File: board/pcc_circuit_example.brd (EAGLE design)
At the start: 52 x 29.1 mm, 18 parts, among them T1 BT138-V

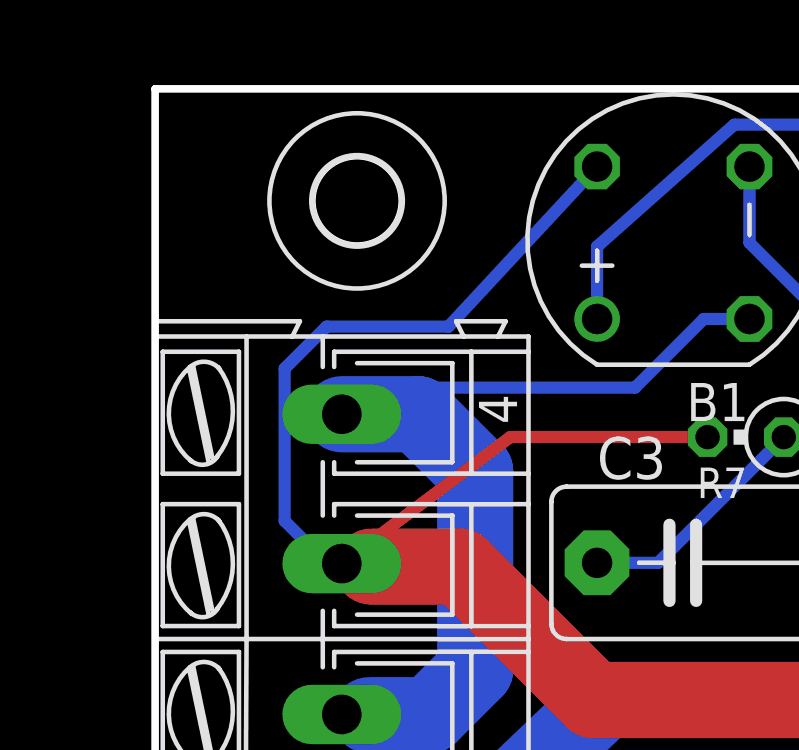
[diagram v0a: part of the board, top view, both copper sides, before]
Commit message: reduce number of drilltools
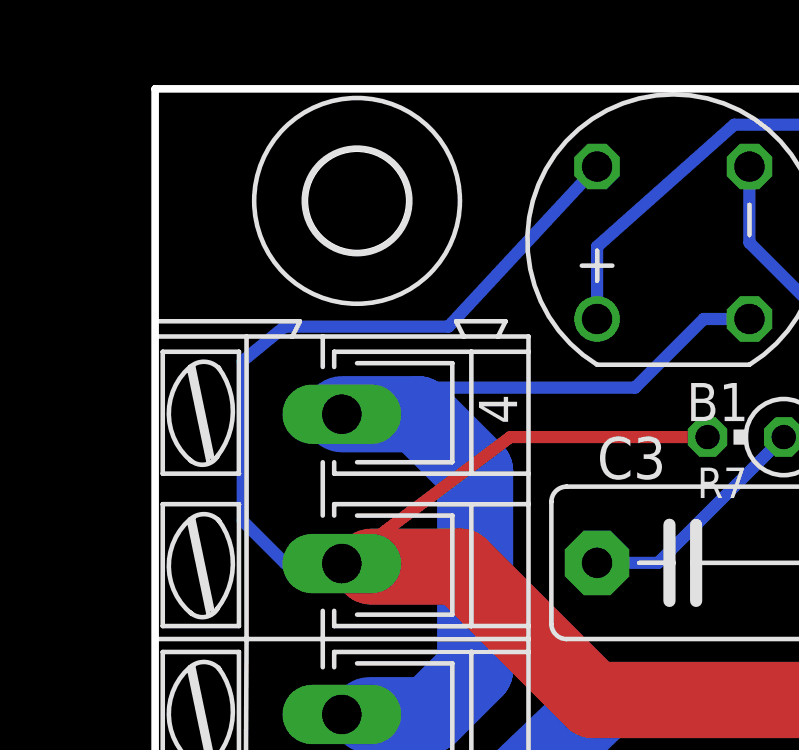
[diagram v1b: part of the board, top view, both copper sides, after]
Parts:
- U$3: device holes:2,8 -> bauteile_jbt:3,3
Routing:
- net AC220V2: track 57.2 -> 60.0 mm
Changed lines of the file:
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@@
 <grid distance="5" unitdist="mil" unit="mil" style="lines" multiple="1" display="yes" altdistance="100" altunitdist="mil" altunit="mil"/>
 <layers>
-<layer number="1" name="Top" color="4" fill="1" visible="yes" active="yes"/>
+<layer number="1" name="Top" color="4" fill="1" visible="no" active="yes"/>
 <layer number="2" name="Route2" color="1" fill="3" visible="no" active="no"/>
 <layer number="3" name="Route3" color="4" fill="3" visible="no" active="no"/>
 <layer number="14" name="Route14" color="1" fill="6" visible="no" active="no"/>
 <layer number="15" name="Route15" color="4" fill="6" visible="no" active="no"/>
-<layer number="16" name="Bottom" color="1" fill="1" visible="no" active="yes"/>
-<layer number="17" name="Pads" color="2" fill="1" visible="no" active="yes"/>
-<layer number="18" name="Vias" color="2" fill="1" visible="no" active="yes"/>
-<layer number="19" name="Unrouted" color="6" fill="1" visible="no" active="yes"/>
+<layer number="16" name="Bottom" color="1" fill="1" visible="yes" active="yes"/>
+<layer number="17" name="Pads" color="2" fill="1" visible="yes" active="yes"/>
+<layer number="18" name="Vias" color="2" fill="1" visible="yes" active="yes"/>
+<layer number="19" name="Unrouted" color="6" fill="1" visible="yes" active="yes"/>
 <layer number="20" name="Dimension" color="15" fill="1" visible="yes" active="yes"/>
-<layer number="21" name="tPlace" color="7" fill="1" visible="yes" active="yes"/>
-<layer number="22" name="bPlace" color="7" fill="1" visible="no" active="yes"/>
+<layer number="21" name="tPlace" color="7" fill="1" visible="no" active="yes"/>
+<layer number="22" name="bPlace" color="7" fill="1" visible="yes" active="yes"/>
 <layer number="23" name="tOrigins" color="15" fill="1" visible="yes" active="yes"/>
-<layer number="24" name="bOrigins" color="15" fill="1" visible="no" active="yes"/>
+<layer number="24" name="bOrigins" color="15" fill="1" visible="yes" active="yes"/>
 <layer number="25" name="tNames" color="7" fill="1" visible="no" active="yes"/>
 <layer number="26" name="bNames" color="7" fill="1" visible="no" active="yes"/>
-<layer number="27" name="tValues" color="7" fill="1" visible="yes" active="yes"/>
-<layer number="28" name="bValues" color="7" fill="1" visible="no" active="yes"/>
-<layer number="29" name="tStop" color="7" fill="3" visible="yes" active="yes"/>
-<layer number="30" name="bStop" color="7" fill="6" visible="no" active="yes"/>
+<layer number="27" name="tValues" color="7" fill="1" visible="no" active="yes"/>
+<layer number="28" name="bValues" color="7" fill="1" visible="yes" active="yes"/>
+<layer number="29" name="tStop" color="7" fill="3" visible="no" active="yes"/>
+<layer number="30" name="bStop" color="7" fill="6" visible="yes" active="yes"/>
 <layer number="31" name="tCream" color="7" fill="4" visible="no" active="yes"/>
 <layer number="32" name="bCream" color="7" fill="5" visible="no" active="yes"/>
@@
 <layer number="37" name="tTest" color="7" fill="1" visible="no" active="yes"/>
 <layer number="38" name="bTest" color="7" fill="1" visible="no" active="yes"/>
-<layer number="39" name="tKeepout" color="4" fill="11" visible="no" active="yes"/>
-<layer number="40" name="bKeepout" color="1" fill="11" visible="no" active="yes"/>
-<layer number="41" name="tRestrict" color="4" fill="10" visible="no" active="yes"/>
-<layer number="42" name="bRestrict" color="1" fill="10" visible="no" active="yes"/>
+<layer number="39" name="tKeepout" color="4" fill="11" visible="yes" active="yes"/>
+<layer number="40" name="bKeepout" color="1" fill="11" visible="yes" active="yes"/>
+<layer number="41" name="tRestrict" color="4" fill="10" visible="yes" active="yes"/>
+<layer number="42" name="bRestrict" color="1" fill="10" visible="yes" active="yes"/>
 <layer number="43" name="vRestrict" color="2" fill="10" visible="no" active="yes"/>
-<layer number="44" name="Drills" color="7" fill="1" visible="yes" active="yes"/>
-<layer number="45" name="Holes" color="7" fill="1" visible="yes" active="yes"/>
-<layer number="46" name="Milling" color="3" fill="1" visible="yes" active="yes"/>
+<layer number="44" name="Drills" color="7" fill="1" visible="no" active="yes"/>
+<layer number="45" name="Holes" color="7" fill="1" visible="no" active="yes"/>
+<layer number="46" name="Milling" color="3" fill="1" visible="no" active="yes"/>
 <layer number="47" name="Measures" color="7" fill="1" visible="no" active="yes"/>
 <layer number="48" name="Document" color="7" fill="1" visible="no" active="yes"/>
@@
 <attribute name="MPN" value="" x="6.223" y="10.795" size="1.778" layer="27" rot="R90" display="off"/>
 </element>
-<element name="U$3" library="holes" package="2,8" value="" x="6.731" y="25.4"/>
+<element name="U$3" library="bauteile_jbt" package="3,3" value="" x="6.731" y="25.4"/>
 <element name="SV1" library="bauteile_jbt" package="FE03-2" value="" x="42.545" y="4.699"/>
 <element name="VCC" library="bauteile_jbt" package="PAD1,6/0,8" value="" x="47.625" y="5.842"/>
@@
 <wire x1="18.415" y1="17.526" x2="11.8364" y2="17.526" width="0.4064" layer="1"/>
 <wire x1="11.8364" y1="17.526" x2="6.223" y2="13.3096" width="0.4064" layer="1"/>
-<wire x1="5.7404" y1="13.3096" x2="4.318" y2="14.732" width="0.4064" layer="16"/>
-<wire x1="4.318" y1="14.732" x2="4.318" y2="19.812" width="0.4064" layer="16"/>
-<wire x1="4.318" y1="19.812" x2="5.715" y2="21.209" width="0.4064" layer="16"/>
-<wire x1="5.715" y1="21.209" x2="9.779" y2="21.209" width="0.4064" layer="16"/>
+<wire x1="4.3434" y1="13.3096" x2="2.921" y2="14.732" width="0.4064" layer="16"/>
+<wire x1="2.921" y1="14.732" x2="2.921" y2="20.066" width="0.4064" layer="16"/>
+<wire x1="2.921" y1="20.066" x2="4.318" y2="21.209" width="0.4064" layer="16"/>
+<wire x1="4.318" y1="21.209" x2="9.779" y2="21.209" width="0.4064" layer="16"/>
 <wire x1="9.779" y1="21.209" x2="14.732" y2="26.543" width="0.4064" layer="16"/>
 <wire x1="23.622" y1="4.445" x2="23.622" y2="7.239" width="2.54" layer="1"/>
@@
 <wire x1="10.16" y1="13.208" x2="7.2136" y2="13.208" width="2.54" layer="1"/>
 <wire x1="7.2136" y1="13.208" x2="6.223" y2="13.3096" width="1.9304" layer="1"/>
-<wire x1="5.7404" y1="13.3096" x2="6.223" y2="13.3096" width="0.4064" layer="16"/>
+<wire x1="4.3434" y1="13.3096" x2="6.223" y2="13.3096" width="0.4064" layer="16"/>
 </signal>
 <signal name="AC220V1">
